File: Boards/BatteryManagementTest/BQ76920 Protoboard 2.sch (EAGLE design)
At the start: 16 parts, among them U1 BQ7692006PWRPW20-M, U2 STD20NF06LDPAK-M

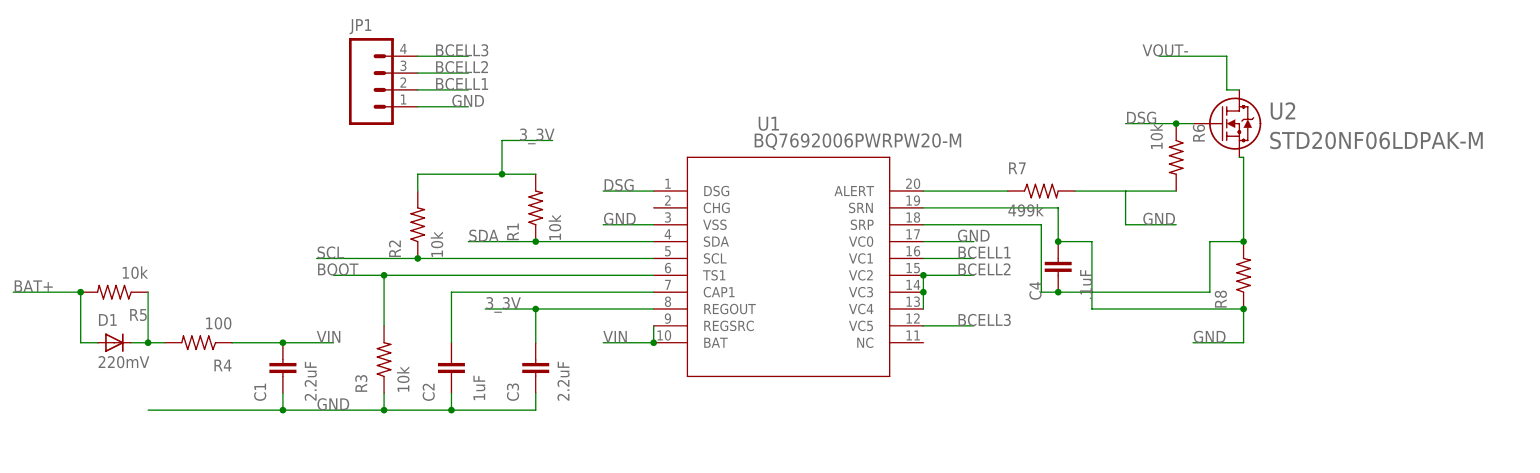
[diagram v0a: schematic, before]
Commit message: added final rev2 protoboard for BQ76920
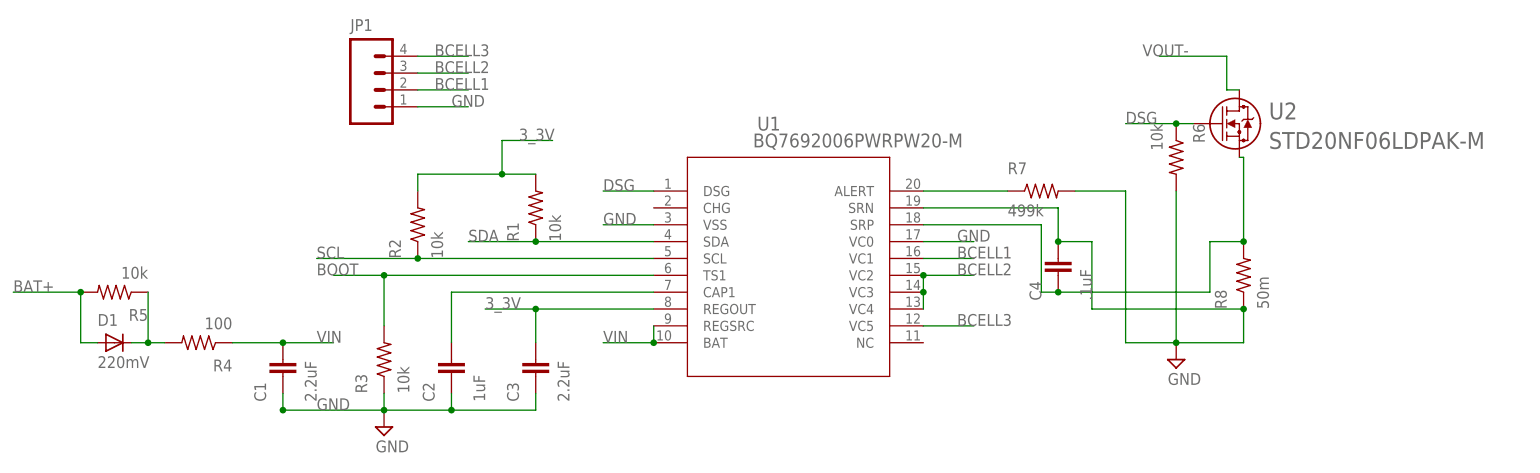
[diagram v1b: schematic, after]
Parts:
- R8: value (none) -> 50m
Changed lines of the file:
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@@
 <part name="D1" library="pie" deviceset="DIODE" device="SOD-323" value="220mV"/>
 <part name="U2" library="pie" deviceset="STD20NF06L" device="DPAK-M"/>
-<part name="R8" library="pie" deviceset="R-US_" device="R2512"/>
+<part name="R8" library="pie" deviceset="R-US_" device="R2512" value="50m"/>
 <part name="R6" library="pie" deviceset="R-US_" device="R0603" value="10k"/>
 <part name="C4" library="pie" deviceset="CAP" device="0603-CAP" value=".1uF"/>
 <part name="R7" library="pie" deviceset="R-US_" device="R0603" value="499k"/>
+<part name="FRAME1" library="pie" deviceset="FRAME_SCHEMATIC" device="">
+<attribute name="AUTHOR" value="Sherwin Afshar"/>
+<attribute name="REVISION" value="2.0"/>
+</part>
+<part name="SUPPLY1" library="pie" deviceset="GND" device=""/>
+<part name="SUPPLY2" library="pie" deviceset="GND" device=""/>
 </parts>
 <sheets>
@@
 <instance part="C4" gate="G$1" x="38.1" y="-2.54" rot="R90"/>
 <instance part="R7" gate="G$1" x="35.56" y="10.16"/>
+<instance part="FRAME1" gate="G$1" x="-132.08" y="-81.28"/>
+<instance part="FRAME1" gate="G$2" x="15.24" y="-81.28">
+<attribute name="AUTHOR" x="15.24" y="-81.28" size="1.778" layer="96" display="both"/>
+<attribute name="REVISION" x="15.24" y="-81.28" size="1.778" layer="96" display="both"/>
+</instance>
+<instance part="SUPPLY1" gate="GND" x="55.88" y="-15.24"/>
+<instance part="SUPPLY2" gate="GND" x="-63.5" y="-25.4"/>
 </instances>
 <busses>
@@
 <label x="-73.66" y="-22.86" size="1.778" layer="95"/>
 <pinref part="C1" gate="G$1" pin="1"/>
-<wire x1="-78.74" y1="-22.86" x2="-99.06" y2="-22.86" width="0.1524" layer="91"/>
 <wire x1="-78.74" y1="-20.32" x2="-78.74" y2="-22.86" width="0.1524" layer="91"/>
 <junction x="-78.74" y="-22.86"/>
+<pinref part="SUPPLY2" gate="GND" pin="GND"/>
 </segment>
 <segment>
 <pinref part="R8" gate="G$1" pin="1"/>
 <wire x1="66.04" y1="-7.62" x2="66.04" y2="-12.7" width="0.1524" layer="91"/>
-<wire x1="66.04" y1="-12.7" x2="58.42" y2="-12.7" width="0.1524" layer="91"/>
-<label x="58.42" y="-12.7" size="1.778" layer="95"/>
 <wire x1="66.04" y1="-7.62" x2="43.18" y2="-7.62" width="0.1524" layer="91"/>
 <wire x1="43.18" y1="-7.62" x2="43.18" y2="2.54" width="0.1524" layer="91"/>
@@
 <pinref part="U1" gate="A" pin="SRN"/>
 <wire x1="38.1" y1="7.62" x2="17.78" y2="7.62" width="0.1524" layer="91"/>
-</segment>
-<segment>
+<wire x1="66.04" y1="-12.7" x2="55.88" y2="-12.7" width="0.1524" layer="91"/>
+<pinref part="R7" gate="G$1" pin="2"/>
+<wire x1="55.88" y1="-12.7" x2="48.26" y2="-12.7" width="0.1524" layer="91"/>
+<wire x1="40.64" y1="10.16" x2="48.26" y2="10.16" width="0.1524" layer="91"/>
+<wire x1="48.26" y1="10.16" x2="48.26" y2="-12.7" width="0.1524" layer="91"/>
 <pinref part="R6" gate="G$1" pin="2"/>
-<wire x1="55.88" y1="10.16" x2="48.26" y2="10.16" width="0.1524" layer="91"/>
-<label x="50.8" y="5.08" size="1.778" layer="95"/>
-<wire x1="48.26" y1="10.16" x2="48.26" y2="5.08" width="0.1524" layer="91"/>
-<wire x1="48.26" y1="5.08" x2="55.88" y2="5.08" width="0.1524" layer="91"/>
-</segment>
-<segment>
-<pinref part="R7" gate="G$1" pin="2"/>
-<wire x1="40.64" y1="10.16" x2="48.26" y2="10.16" width="0.1524" layer="91"/>
+<wire x1="55.88" y1="10.16" x2="55.88" y2="-12.7" width="0.1524" layer="91"/>
+<junction x="55.88" y="-12.7"/>
+<pinref part="SUPPLY1" gate="GND" pin="GND"/>
 </segment>
 </net>
